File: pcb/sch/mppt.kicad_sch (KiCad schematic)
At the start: 33 parts, among them Q5 BSC014, Q6 BSC014, Q7 BSC014, Q8 BSC014, Q9 BSC014, U1 BQ25798

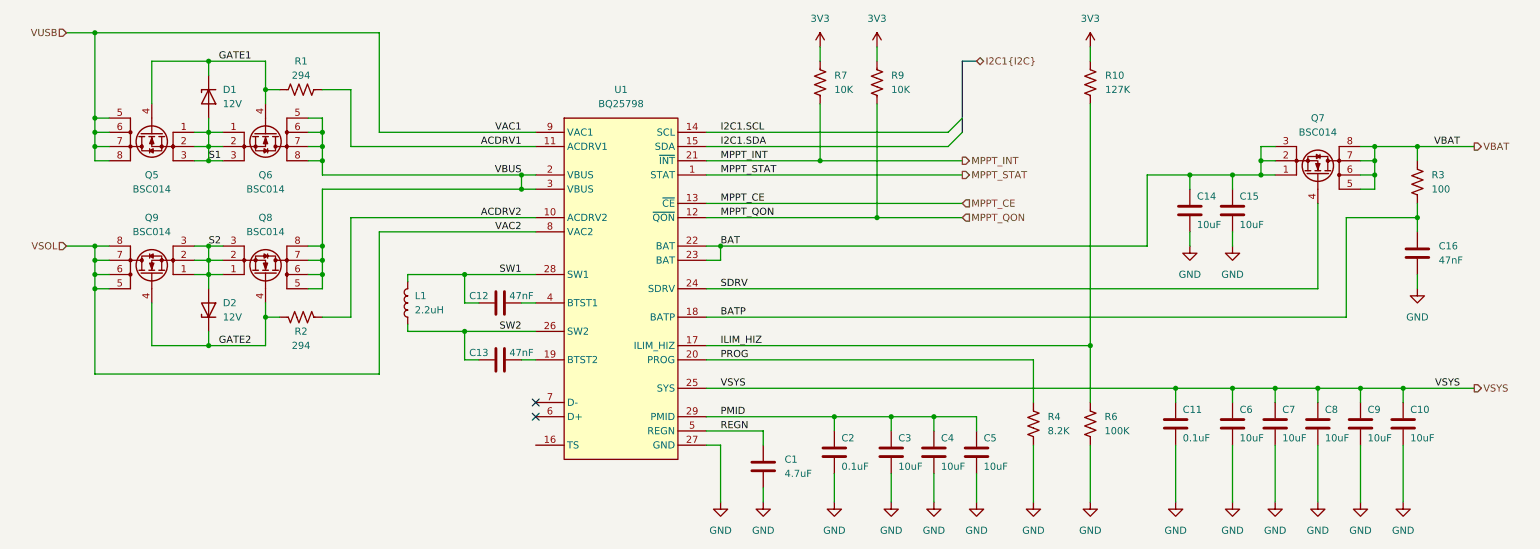
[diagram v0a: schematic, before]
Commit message: add mcu hierarchy, rgb led, stm32 pinouts
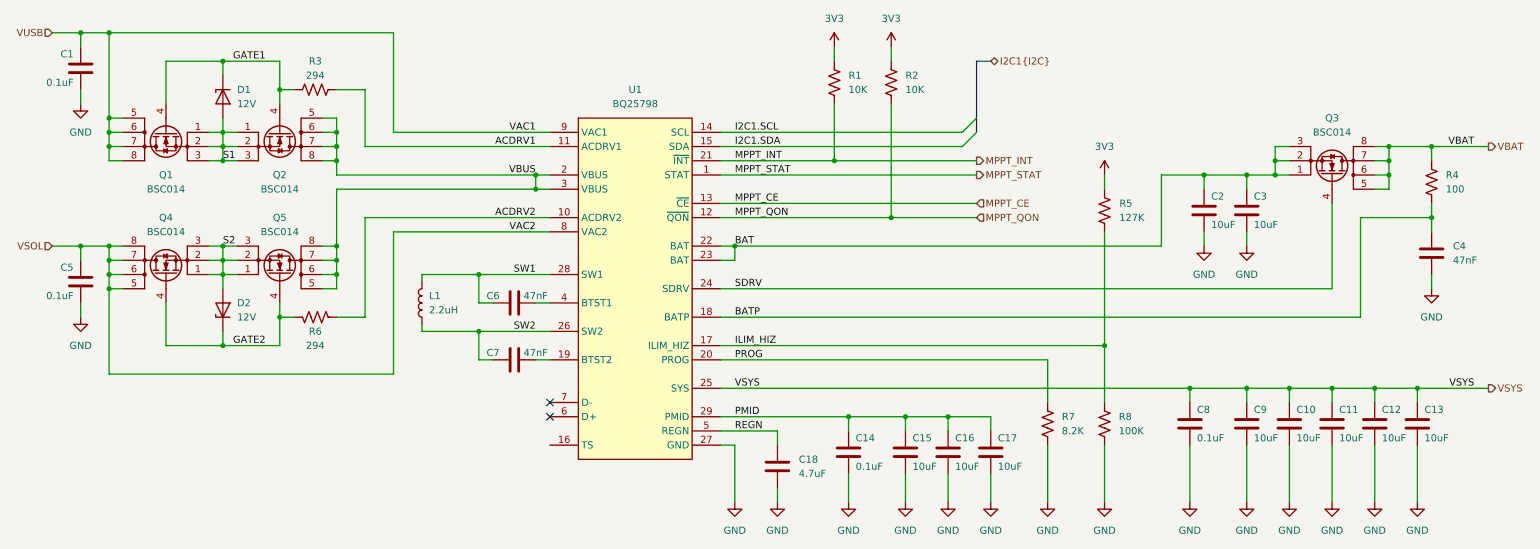
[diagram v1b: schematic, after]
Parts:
- added C1, C5: 0.1uF, Capacitor_SMD:C_0402_1005Metric, symbol Device:C
- renumbered C7 to C10, C8 to C11, C9 to C12, C10 to C13, C2 to C14, C3 to C15, C4 to C16, C5 to C17, C1 to C18, C14 to C2, C15 to C3, C16 to C4, C12 to C6, C13 to C7, C11 to C8, C6 to C9, Q5 to Q1, Q6 to Q2, Q7 to Q3, Q9 to Q4, Q8 to Q5, R7 to R1, R9 to R2, R1 to R3, R3 to R4, R10 to R5, R2 to R6, R4 to R7, R6 to R8
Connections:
- net GND: now also C1.2, C5.2
- net VSOL: now also C5.1
- net VUSB: now also C1.1
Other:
- moved on the sheet: C10, C11, C12, C13, C14, C15, C16, C17, C18, C2, C3, C4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
